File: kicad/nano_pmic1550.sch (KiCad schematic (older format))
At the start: 53 parts, among them J2 PMIC_I2C, J7 LiPo_THM, Q1 2SK3018, U6 PF1550

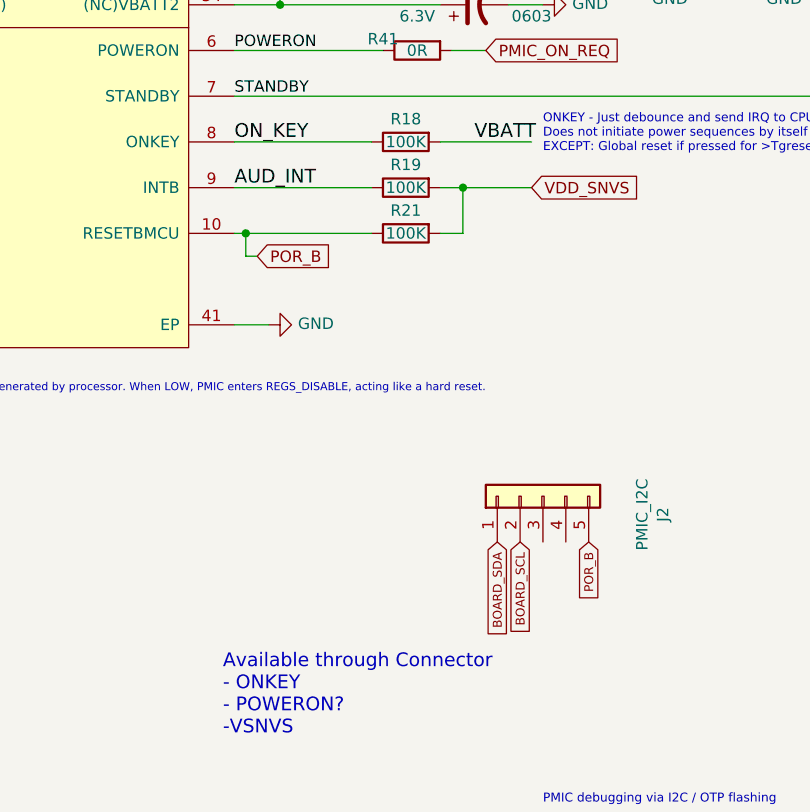
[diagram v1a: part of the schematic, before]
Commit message: pmic_int connection
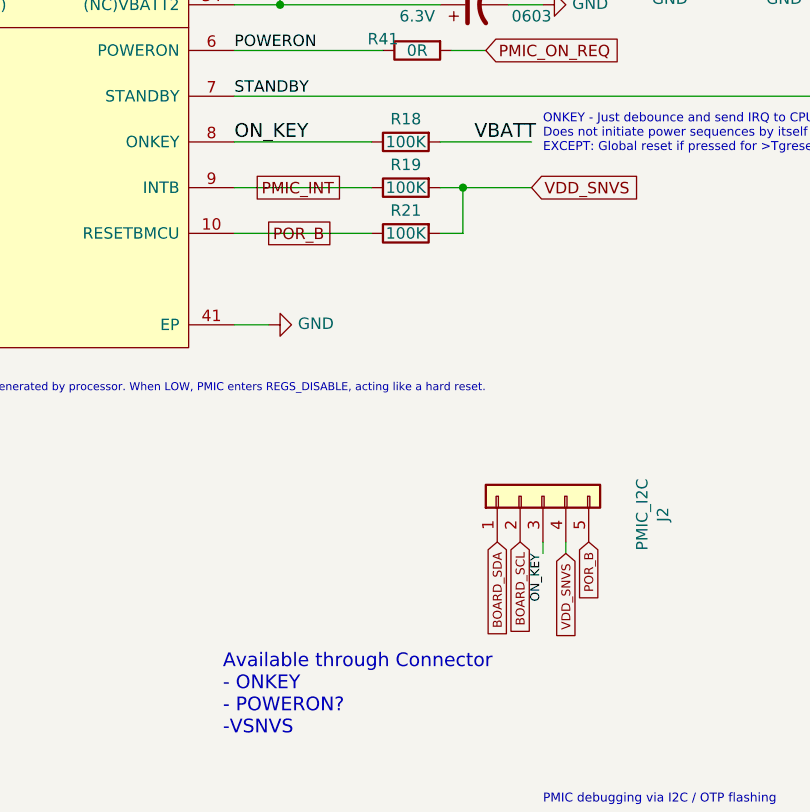
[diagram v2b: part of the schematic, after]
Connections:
- net ON_KEY: now also J2.3 (Pin_3)
- net VDD_SNVS: now also J2.4 (Pin_4)
- net AUD_INT renamed PMIC_INT
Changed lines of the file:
@@
 	0    -1   1    0
 $EndComp
-Text Label 4250 4900 0    60   ~ 0
-AUD_INT
 $Comp
 L nano-rescue:R R?
@@
 Wire Wire Line
 	4250 4700 4850 4700
-Wire Wire Line
-	4250 4900 4850 4900
-Wire Wire Line
-	4250 5100 4300 5100
 $Comp
 L nano-rescue:R R?
@@
 Text GLabel 5500 6450 3    39   Input ~ 0
 BOARD_SCL
-Text GLabel 4350 5200 2    50   Input ~ 0
+Text GLabel 4400 5100 2    50   UnSpc ~ 0
 POR_B
-Wire Wire Line
-	4350 5200 4300 5200
-Wire Wire Line
-	4300 5200 4300 5100
-Connection ~ 4300 5100
-Wire Wire Line
-	4300 5100 4850 5100
 Text GLabel 5800 6450 3    39   Input ~ 0
 POR_B
@@
 Text Notes 7050 4700 0    50   ~ 0
 TODO:\nONKEY add SMD Switch 3.0 x 2.0 mm
+Text GLabel 4350 4900 2    50   UnSpc ~ 0
+PMIC_INT
+Wire Wire Line
+	4250 4900 4850 4900
+Wire Wire Line
+	4250 5100 4850 5100
+Text Label 5600 6500 3    39   ~ 0
+ON_KEY
+Wire Wire Line
+	5700 6450 5700 6500
+Wire Wire Line
+	5600 6450 5600 6500
+Text GLabel 5700 6500 3    39   Input ~ 0
+VDD_SNVS
 $EndSCHEMATC
